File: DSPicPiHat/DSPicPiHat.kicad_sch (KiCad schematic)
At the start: 82 parts, among them J1 Conn_01x09_Female, J4 Conn_PIC_ICSP_ICD, J5 USB_C_Receptacle_USB2.0, J6 PowerInput, J8 RasPiHeaders, SW1 POWER_Select, SW2 SW_DIP_x08, U1 DSPIC33CH512MP508T-I_PT, U10 DF5A6.2CJE_LM, U11 FT230XS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

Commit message: Moved fuse to be after the PSU switch
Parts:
- removed F1: 3.5 A(?), Fuse:Fuse_2920_7451Metric, symbol Device:Polyfuse_Small
- added F?: 3.5 A(?), Fuse:Fuse_2920_7451Metric, symbol Device:Polyfuse_Small
- added J2: Conn_01x04_Female, Connector_JST:JST_SH_BM04B-SRSS-TB_1x04-1MP_P1.00mm_Vertical, symbol Connector:Conn_01x04_Female
- L1: value 10 mA <1o -> 6.33 mH
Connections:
- net +5V: now also F?.2, J2.2 (Pin_2); no longer SW1.2 (B)
- net GND: now also J2.1 (Pin_1)
- net PI_I2C_SCL: now also J2.4 (Pin_4)
- net PI_I2C_SDA: now also J2.3 (Pin_3)
- net VBUS_USBC: now also FB1.2
- new net: F?.1, SW1.2 (B)
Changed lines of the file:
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@@
     (stroke (width 0) (type default) (color 0 0 0 0))
   )
+  (wire (pts (xy 369.57 161.29) (xy 372.11 161.29))
+    (stroke (width 0) (type default) (color 0 0 0 0))
+  )
   (wire (pts (xy 377.19 36.83) (xy 378.46 36.83))
     (stroke (width 0) (type default) (color 0 0 0 0))
@@
     (stroke (width 0) (type default) (color 0 0 0 0))
   )
-  (wire (pts (xy 367.03 193.04) (xy 377.19 193.04))
-    (stroke (width 0) (type default) (color 0 0 0 0))
-  )
   (wire (pts (xy 367.03 76.2) (xy 368.3 76.2))
     (stroke (width 0) (type default) (color 0 0 0 0))
@@
     (stroke (width 0) (type default) (color 0 0 0 0))
   )
+  (wire (pts (xy 363.22 161.29) (xy 364.49 161.29))
+    (stroke (width 0) (type default) (color 0 0 0 0))
+  )
   (polyline (pts (xy 290.83 177.8) (xy 290.83 251.46))
     (stroke (width 0) (type default) (color 0 0 0 0))
@@
     (stroke (width 0) (type default) (color 0 0 0 0))
   )
-  (wire (pts (xy 354.33 193.04) (xy 361.95 193.04))
+  (wire (pts (xy 354.33 193.04) (xy 377.19 193.04))
     (stroke (width 0) (type default) (color 0 0 0 0))
   )
@@
     (stroke (width 0) (type default) (color 0 0 0 0))
   )
-  (wire (pts (xy 363.22 161.29) (xy 372.11 161.29))
-    (stroke (width 0) (type default) (color 0 0 0 0))
-  )
   (wire (pts (xy 349.25 207.01) (xy 341.63 207.01))
     (stroke (width 0) (type default) (color 0 0 0 0))
@@
     )
   )
+  (global_label "PI_I2C_SCL" (shape input) (at 303.53 113.03 180) (fields_autoplaced)
+    (effects (font (size 1.27 1.27)) (justify right))
+    (property "Intersheet References" "${INTERSHEET_REFS}" (id 0) (at 290.715 113.1094 0)
+      (effects (font (size 1.27 1.27)) (justify right) hide)
+    )
+  )
   (global_label "U1RX" (shape input) (at 71.12 29.21 0) (fields_autoplaced)
     (effects (font (size 1.27 1.27)) (justify left))
@@
     )
   )
+  (global_label "PI_I2C_SDA" (shape input) (at 303.53 110.49 180) (fields_autoplaced)
+    (effects (font (size 1.27 1.27)) (justify right))
+    (property "Intersheet References" "${INTERSHEET_REFS}" (id 0) (at 290.6545 110.5694 0)
+      (effects (font (size 1.27 1.27)) (justify right) hide)
+    )
+  )
   (global_label "EXT_Z_PWM_01" (shape input) (at 144.78 270.51 180) (fields_autoplaced)
     (effects (font (size 1.27 1.27)) (justify right))
@@
     (pin "4")
   )
-  (symbol (lib_id "Device:Polyfuse_Small") (at 364.49 193.04 90) (unit 1)
-    (in_bom yes) (on_board yes) (fields_autoplaced)
-    (property "Reference" "F1" (id 0) (at 364.49 186.69 90))
-    (property "Value" "3.5 A(?)" (id 1) (at 364.49 189.23 90))
-    (property "Footprint" "Fuse:Fuse_2920_7451Metric" (id 2) (at 369.57 191.77 0)
-      (effects (font (size 1.27 1.27)) (justify left) hide)
-    )
-    (property "Datasheet" "~" (id 3) (at 364.49 193.04 0)
-      (effects (font (size 1.27 1.27)) hide)
-    )
-    (pin "1")
-    (pin "2")
-  )
   (symbol (lib_id "Device:R_Small") (at 52.07 234.95 0) (unit 1)
     (in_bom yes) (on_board yes) (fields_autoplaced)
@@
     (pin "1")
   )
+  (symbol (lib_id "power:GND") (at 303.53 105.41 270) (unit 1)
+    (in_bom yes) (on_board yes)
+    (property "Reference" "#PWR0110" (id 0) (at 297.18 105.41 0)
+      (effects (font (size 1.27 1.27)) hide)
+    )
+    (property "Value" "GND" (id 1) (at 299.72 106.68 0)
+      (effects (font (size 1.27 1.27)) (justify right))
+    )
+    (property "Footprint" "" (id 2) (at 303.53 105.41 0)
+      (effects (font (size 1.27 1.27)) hide)
+    )
+    (property "Datasheet" "" (id 3) (at 303.53 105.41 0)
+      (effects (font (size 1.27 1.27)) hide)
+    )
+    (pin "1")
+  )
   (symbol (lib_id "Device:LED") (at 273.05 213.36 180) (unit 1)
     (in_bom yes) (on_board yes)
@@
     (pin "1")
   )
+  (symbol (lib_id "power:+5V") (at 303.53 107.95 90) (unit 1)
+    (in_bom yes) (on_board yes)
+    (property "Reference" "#PWR0109" (id 0) (at 307.34 107.95 0)
+      (effects (font (size 1.27 1.27)) hide)
+    )
+    (property "Value" "+5V" (id 1) (at 298.45 107.95 90))
+    (property "Footprint" "" (id 2) (at 303.53 107.95 0)
+      (effects (font (size 1.27 1.27)) hide)
+    )
+    (property "Datasheet" "" (id 3) (at 303.53 107.95 0)
+      (effects (font (size 1.27 1.27)) hide)
+    )
+    (pin "1")
+  )
   (symbol (lib_id "power:GND") (at 389.89 123.19 180) (unit 1)
     (in_bom yes) (on_board yes)
@@
     (pin "2")
   )
+  (symbol (lib_id "Device:Polyfuse_Small") (at 367.03 161.29 90) (unit 1)
+    (in_bom yes) (on_board yes) (fields_autoplaced)
+    (property "Reference" "F?" (id 0) (at 367.03 154.94 90))
+    (property "Value" "3.5 A(?)" (id 1) (at 367.03 157.48 90))
+    (property "Footprint" "Fuse:Fuse_2920_7451Metric" (id 2) (at 372.11 160.02 0)
+      (effects (font (size 1.27 1.27)) (justify left) hide)
+    )
+    (property "Datasheet" "~" (id 3) (at 367.03 161.29 0)
+      (effects (font (size 1.27 1.27)) hide)
+    )
+    (pin "1")
+    (pin "2")
+  )
   (symbol (lib_id "power:GND") (at 97.79 280.67 0) (unit 1)
     (in_bom yes) (on_board yes)
@@
     (in_bom yes) (on_board yes) (fields_autoplaced)
     (property "Reference" "L1" (id 0) (at 148.59 104.14 90))
-    (property "Value" "10 mA <1o" (id 1) (at 148.59 106.68 90))
+    (property "Value" "6.33 mH" (id 1) (at 148.59 106.68 90))
     (property "Footprint" "Inductor_SMD:L_0805_2012Metric" (id 2) (at 148.59 110.49 0)
       (effects (font (size 1.27 1.27)) hide)
@@
     (pin "1")
   )
+  (symbol (lib_id "Connector:Conn_01x04_Female") (at 308.61 107.95 0) (unit 1)
+    (in_bom yes) (on_board yes) (fields_autoplaced)
+    (property "Reference" "J2" (id 0) (at 309.88 107.9499 0)
+      (effects (font (size 1.27 1.27)) (justify left))
+    )
+    (property "Value" "Conn_01x04_Female" (id 1) (at 309.88 110.4899 0)
+      (effects (font (size 1.27 1.27)) (justify left))
+    )
+    (property "Footprint" "Connector_JST:JST_SH_BM04B-SRSS-TB_1x04-1MP_P1.00mm_Vertical" (id 2) (at 308.61 107.95 0)
+      (effects (font (size 1.27 1.27)) hide)
+    )
+    (property "Datasheet" "~" (id 3) (at 308.61 107.95 0)
+      (effects (font (size 1.27 1.27)) hide)
+    )
+    (pin "1")
+    (pin "2")
+    (pin "3")
+    (pin "4")
+  )
   (symbol (lib_id "power:GND") (at 300.99 231.14 0) (unit 1)
     (in_bom yes) (on_board yes) (fields_autoplaced)
@@
       (reference "#PWR0108") (unit 1) (value "GND") (footprint "")
     )
+    (path "/5f9efb95-5c0c-4aee-89de-c55a683eb7fc"
+      (reference "#PWR0109") (unit 1) (value "+5V") (footprint "")
+    )
+    (path "/27b6aebd-f2d2-4fdc-9719-f31a8e7f837b"
+      (reference "#PWR0110") (unit 1) (value "GND") (footprint "")
+    )
     (path "/bcc72ff3-f25f-4fbf-8751-185f0084a0a5"
       (reference "#PWR0111") (unit 1) (value "GND") (footprint "")
@@
       (reference "D13") (unit 1) (value "WS2812B") (footprint "LED_SMD:LED_WS2812B-2020_PLCC4_2.0x2.0mm")
     )
-    (path "/0b60c446-5161-421b-a91b-bda5e4f17126"
-      (reference "F1") (unit 1) (value "3.5 A(?)") (footprint "Fuse:Fuse_2920_7451Metric")
+    (path "/6c4fc749-d06c-4285-ad23-6e82f5e07688"
+      (reference "F?") (unit 1) (value "3.5 A(?)") (footprint "Fuse:Fuse_2920_7451Metric")
     )
     (path "/73568451-6492-491a-bea8-1d81af82b417"
@@
       (reference "J1") (unit 1) (value "Conn_01x09_Female") (footprint "Connector_PinHeader_2.54mm:PinHeader_1x09_P2.54mm_Vertical")
     )
+    (path "/d6afa4ac-5290-40e6-9de7-f713368db060"
+      (reference "J2") (unit 1) (value "Conn_01x04_Female") (footprint "Connector_JST:JST_SH_BM04B-SRSS-TB_1x04-1MP_P1.00mm_Vertical")
+    )
     (path "/5662e14b-7d70-457a-a9d1-e3f8a620952f"
       (reference "J4") (unit 1) (value "Conn_PIC_ICSP_ICD") (footprint "Connector_PinHeader_2.54mm:PinHeader_2x03_P2.54mm_Vertical")
@@
     )
     (path "/ca6ebcb9-dea8-48fc-a195-579c78ac092e"
-      (reference "L1") (unit 1) (value "10 mA <1o") (footprint "Inductor_SMD:L_0805_2012Metric")
+      (reference "L1") (unit 1) (value "6.33 mH") (footprint "Inductor_SMD:L_0805_2012Metric")
     )
     (path "/0b9a31a6-19fd-4fe4-86f5-2dae5bff4030"

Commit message: oops
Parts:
- gave numbers to parts that had none: 1
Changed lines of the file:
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@@
   (symbol (lib_id "Device:Polyfuse_Small") (at 367.03 161.29 90) (unit 1)
     (in_bom yes) (on_board yes) (fields_autoplaced)
-    (property "Reference" "F?" (id 0) (at 367.03 154.94 90))
+    (property "Reference" "F1" (id 0) (at 367.03 154.94 90))
     (property "Value" "3.5 A(?)" (id 1) (at 367.03 157.48 90))
     (property "Footprint" "Fuse:Fuse_2920_7451Metric" (id 2) (at 372.11 160.02 0)
@@
     )
     (path "/6c4fc749-d06c-4285-ad23-6e82f5e07688"
-      (reference "F?") (unit 1) (value "3.5 A(?)") (footprint "Fuse:Fuse_2920_7451Metric")
+      (reference "F1") (unit 1) (value "3.5 A(?)") (footprint "Fuse:Fuse_2920_7451Metric")
     )
     (path "/73568451-6492-491a-bea8-1d81af82b417"

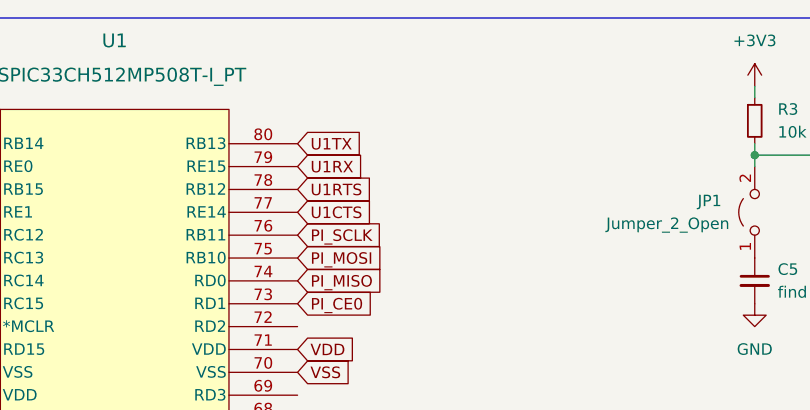
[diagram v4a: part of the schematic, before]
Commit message: added o ohm resistors based on braincodec's rx tx switcher
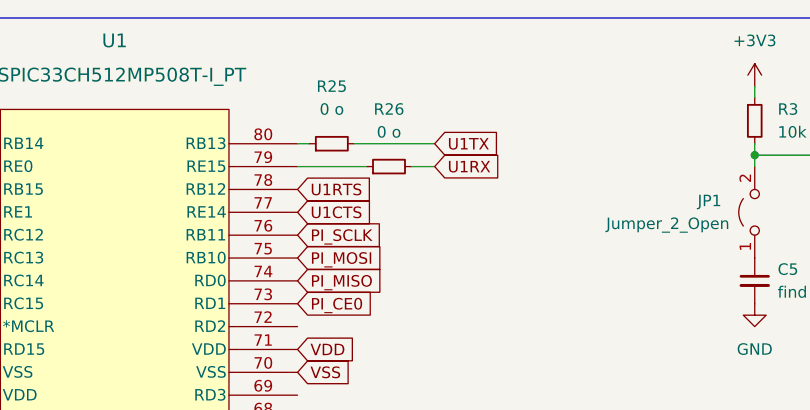
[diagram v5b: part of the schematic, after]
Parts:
- added R25, R26: 0 o, Resistor_SMD:R_0805_2012Metric, symbol Device:R_Small
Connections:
- net U1RX: now also R26.2; no longer U1.79 (RE15)
- net U1TX: now also R25.2; no longer U1.80 (RB13)
- new net: R25.1, U1.80 (RB13)
- new net: R26.1, U1.79 (RE15)
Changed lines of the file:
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@@
     (stroke (width 0) (type default) (color 0 0 0 0))
   )
+  (wire (pts (xy 71.12 26.67) (xy 72.39 26.67))
+    (stroke (width 0) (type default) (color 0 0 0 0))
+  )
   (wire (pts (xy 370.84 67.31) (xy 370.84 78.74))
     (stroke (width 0) (type default) (color 0 0 0 0))
@@
     (stroke (width 0) (type default) (color 0 0 0 0))
   )
+  (wire (pts (xy 83.82 29.21) (xy 86.36 29.21))
+    (stroke (width 0) (type default) (color 0 0 0 0))
+  )
   (polyline (pts (xy 250.19 207.01) (xy 250.19 257.81))
     (stroke (width 0) (type default) (color 0 0 0 0))
@@
     (stroke (width 0) (type default) (color 0 0 0 0))
   )
+  (wire (pts (xy 77.47 26.67) (xy 86.36 26.67))
+    (stroke (width 0) (type default) (color 0 0 0 0))
+  )
   (polyline (pts (xy 68.58 242.57) (xy 68.58 284.48))
     (stroke (width 0) (type default) (color 0 0 0 0))
@@
     (stroke (width 0) (type default) (color 0 0 0 0))
   )
+  (wire (pts (xy 71.12 29.21) (xy 78.74 29.21))
+    (stroke (width 0) (type default) (color 0 0 0 0))
+  )
   (wire (pts (xy 276.86 220.98) (xy 279.4 220.98))
     (stroke (width 0) (type default) (color 0 0 0 0))
@@
     )
   )
-  (global_label "U1TX" (shape input) (at 71.12 26.67 0) (fields_autoplaced)
+  (global_label "U1TX" (shape input) (at 86.36 26.67 0) (fields_autoplaced)
     (effects (font (size 1.27 1.27)) (justify left))
-    (property "Intersheet References" "${INTERSHEET_REFS}" (id 0) (at 78.2502 26.5906 0)
+    (property "Intersheet References" "${INTERSHEET_REFS}" (id 0) (at 93.4902 26.5906 0)
       (effects (font (size 1.27 1.27)) (justify left) hide)
     )
@@
     )
   )
-  (global_label "U1TX" (shape input) (at 397.51 200.66 0) (fields_autoplaced)
-    (effects (font (size 1.27 1.27)) (justify left))
-    (property "Intersheet References" "${INTERSHEET_REFS}" (id 0) (at 404.6402 200.5806 0)
-      (effects (font (size 1.27 1.27)) (justify left) hide)
-    )
-  )
   (global_label "AVDD" (shape input) (at 167.64 105.41 180) (fields_autoplaced)
     (effects (font (size 1.27 1.27)) (justify right))
@@
     )
   )
+  (global_label "U1TX" (shape input) (at 397.51 200.66 0) (fields_autoplaced)
+    (effects (font (size 1.27 1.27)) (justify left))
+    (property "Intersheet References" "${INTERSHEET_REFS}" (id 0) (at 404.6402 200.5806 0)
+      (effects (font (size 1.27 1.27)) (justify left) hide)
+    )
+  )
   (global_label "EXT_Y_PWM_00" (shape input) (at 107.95 270.51 0) (fields_autoplaced)
     (effects (font (size 1.27 1.27)) (justify left))
@@
     )
   )
-  (global_label "U1RX" (shape input) (at 71.12 29.21 0) (fields_autoplaced)
+  (global_label "U1RX" (shape input) (at 86.36 29.21 0) (fields_autoplaced)
     (effects (font (size 1.27 1.27)) (justify left))
-    (property "Intersheet References" "${INTERSHEET_REFS}" (id 0) (at 78.5526 29.1306 0)
+    (property "Intersheet References" "${INTERSHEET_REFS}" (id 0) (at 93.7926 29.1306 0)
       (effects (font (size 1.27 1.27)) (justify left) hide)
     )
@@
     (pin "2")
   )
+  (symbol (lib_id "Device:R_Small") (at 74.93 26.67 90) (unit 1)
+    (in_bom yes) (on_board yes) (fields_autoplaced)
+    (property "Reference" "R25" (id 0) (at 74.93 20.32 90))
+    (property "Value" "0 o" (id 1) (at 74.93 22.86 90))
+    (property "Footprint" "Resistor_SMD:R_0805_2012Metric" (id 2) (at 74.93 26.67 0)
+      (effects (font (size 1.27 1.27)) hide)
+    )
+    (property "Datasheet" "~" (id 3) (at 74.93 26.67 0)
+      (effects (font (size 1.27 1.27)) hide)
+    )
+    (pin "1")
+    (pin "2")
+  )
   (symbol (lib_id "power:GND") (at 45.72 190.5 0) (unit 1)
     (in_bom yes) (on_board yes) (fields_autoplaced)
@@
     (pin "1")
   )
+  (symbol (lib_id "Device:R_Small") (at 81.28 29.21 90) (unit 1)
+    (in_bom yes) (on_board yes) (fields_autoplaced)
+    (property "Reference" "R26" (id 0) (at 81.28 22.86 90))
+    (property "Value" "0 o" (id 1) (at 81.28 25.4 90))
+    (property "Footprint" "Resistor_SMD:R_0805_2012Metric" (id 2) (at 81.28 29.21 0)
+      (effects (font (size 1.27 1.27)) hide)
+    )
+    (property "Datasheet" "~" (id 3) (at 81.28 29.21 0)
+      (effects (font (size 1.27 1.27)) hide)
+    )
+    (pin "1")
+    (pin "2")
+  )
   (symbol (lib_id "power:GND") (at 172.72 25.4 90) (unit 1)
     (in_bom yes) (on_board yes) (fields_autoplaced)
@@
       (reference "R24") (unit 1) (value "10k") (footprint "Resistor_SMD:R_0805_2012Metric")
     )
+    (path "/7d947c7c-182e-4ac4-97c5-da6a2fb3c10c"
+      (reference "R25") (unit 1) (value "0 o") (footprint "Resistor_SMD:R_0805_2012Metric")
+    )
+    (path "/aaf0ff05-328a-4444-8ccf-74f84a76e126"
+      (reference "R26") (unit 1) (value "0 o") (footprint "Resistor_SMD:R_0805_2012Metric")
+    )
     (path "/37384411-5ee2-41ac-988a-311835386196"

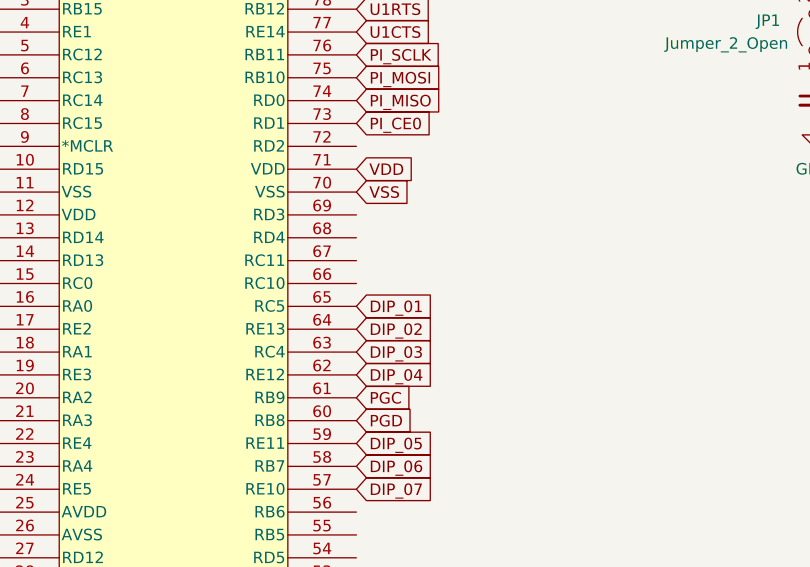
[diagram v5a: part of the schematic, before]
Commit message: dip_00 was unconnected, working through drc errors and warnings.
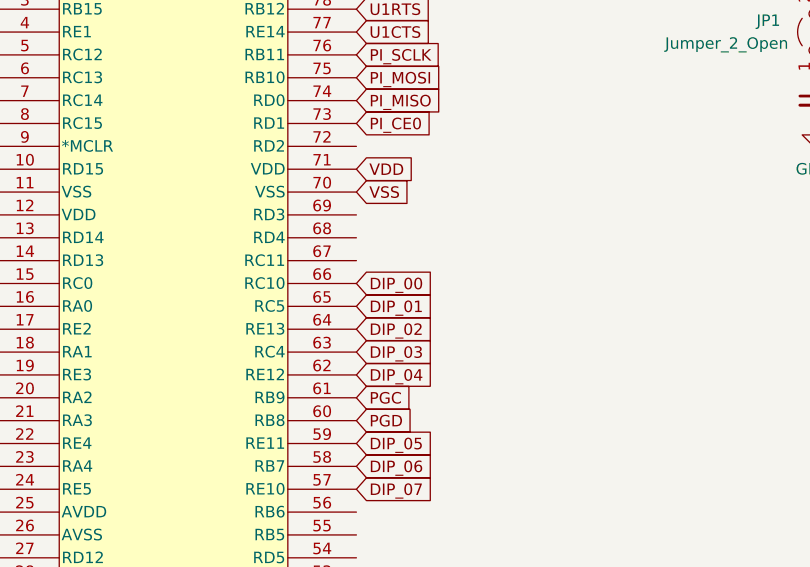
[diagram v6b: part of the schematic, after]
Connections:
- net DIP_00: now also U1.66 (RC10)
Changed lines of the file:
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@@
+    )
+  )
+  (global_label "DIP_00" (shape input) (at 71.12 62.23 0) (fields_autoplaced)
+    (effects (font (size 1.27 1.27)) (justify left))
+    (property "Intersheet References" "${INTERSHEET_REFS}" (id 0) (at 80.0645 62.1506 0)
+      (effects (font (size 1.27 1.27)) (justify left) hide)
     )
   )

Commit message: organized schem
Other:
- note added: "I2C headers"
- moved on the sheet: C10, C11, C12, C6, C9, J2, J4, L1
